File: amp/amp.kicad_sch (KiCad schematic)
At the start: 40 parts, among them J1 Input, J2 Speaker 8Ω, J3 Headphones, J6 FX Send, J7 FX Return, SW1 FX Enable/Bypass, U1 NE5532, U3 LM386

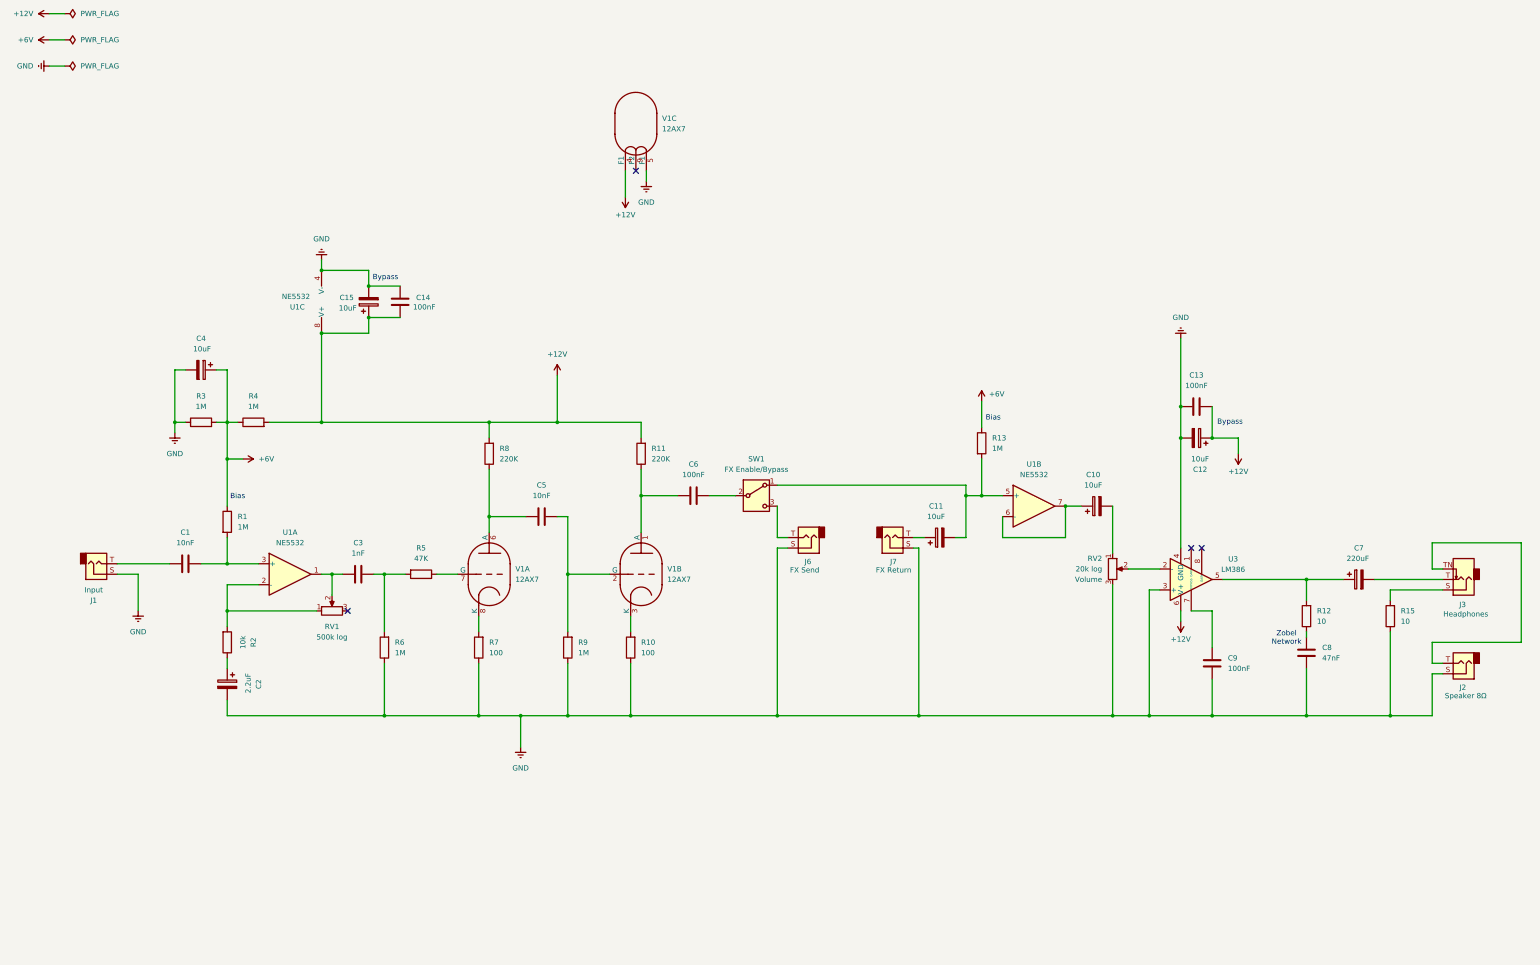
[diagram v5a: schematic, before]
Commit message: Add power control and led indicators
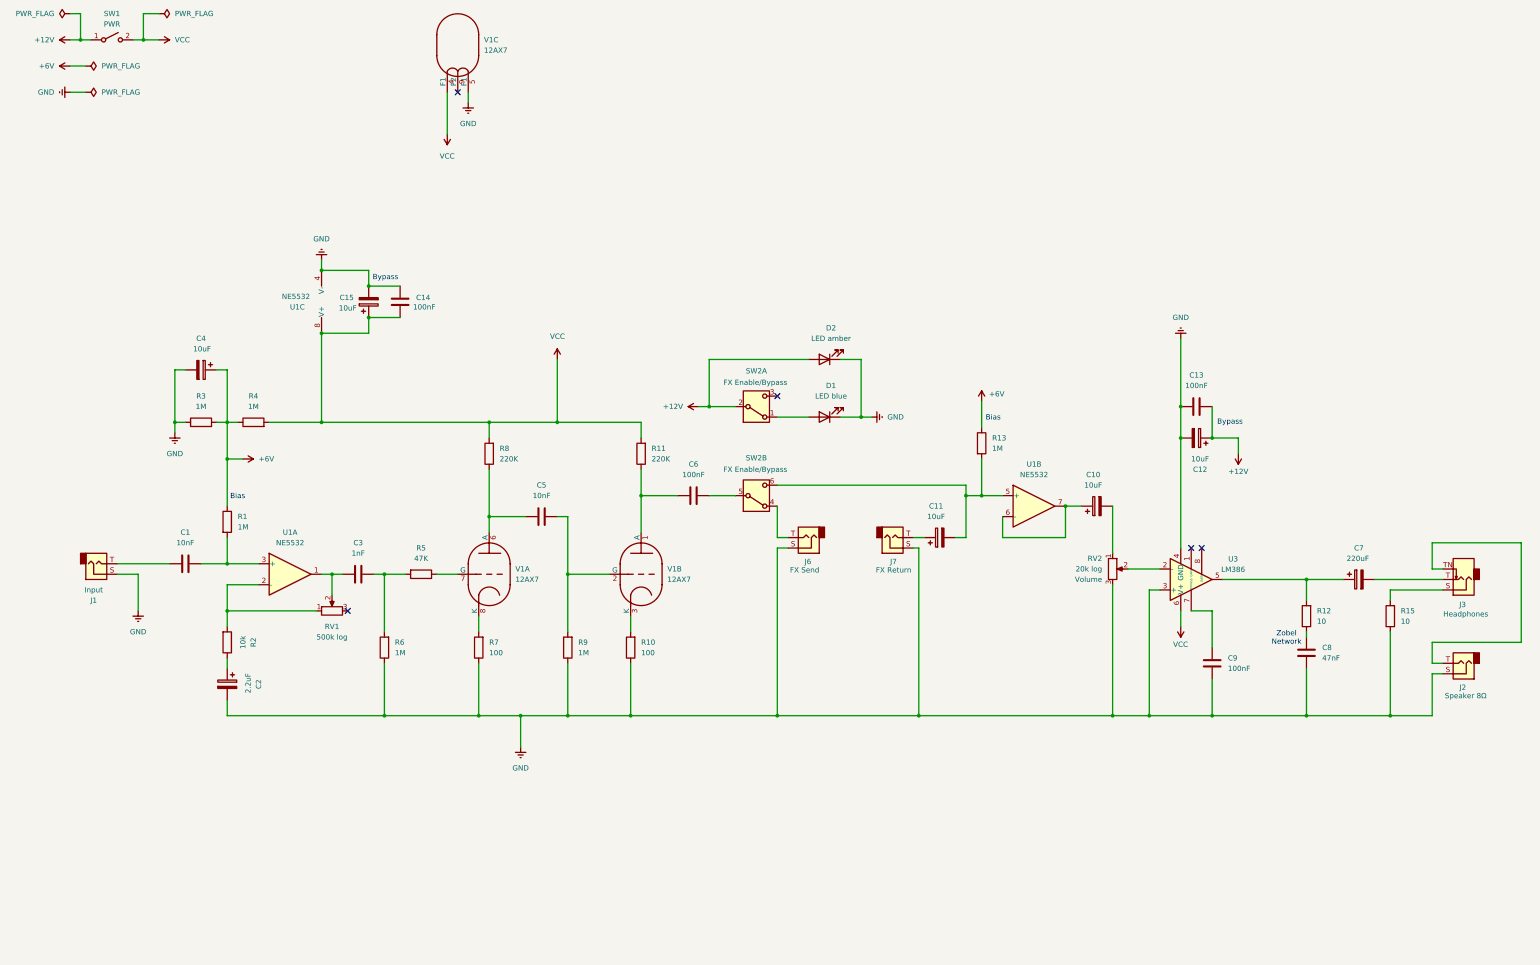
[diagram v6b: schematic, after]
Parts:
- removed SW1: FX Enable/Bypass, symbol Switch:SW_SPDT
- added D1: LED blue, symbol Device:LED
- added D2: LED amber, symbol Device:LED
- added SW1: PWR, symbol Switch:SW_SPST
- added SW2: FX Enable/Bypass, symbol Switch:SW_DPDT_x2
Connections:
- net +12V: now also D2.2 (A), SW1.1 (A), SW2.2 (B); no longer C14.2, C15.1, R11.2, R4.2, R8.2, U1.8 (V+), U3.6 (V+), V1.4 (F1)
- net GND: now also D1.1 (K), D2.1 (K)
- net at J6.T: now also SW2.4 (A)
- net at C6.2: now also SW2.5 (B)
- net at C11.2, R13.2, U1.5 (+): now also SW2.6 (C)
- new net: D1.2 (A), SW2.1 (A)
- new net VCC: C14.2, C15.1, R11.2, R4.2, R8.2, SW1.2 (B), U1.8 (V+), U3.6 (V+), V1.4 (F1)
- no-connect marks 4 -> 5
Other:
- moved on the sheet: V1C

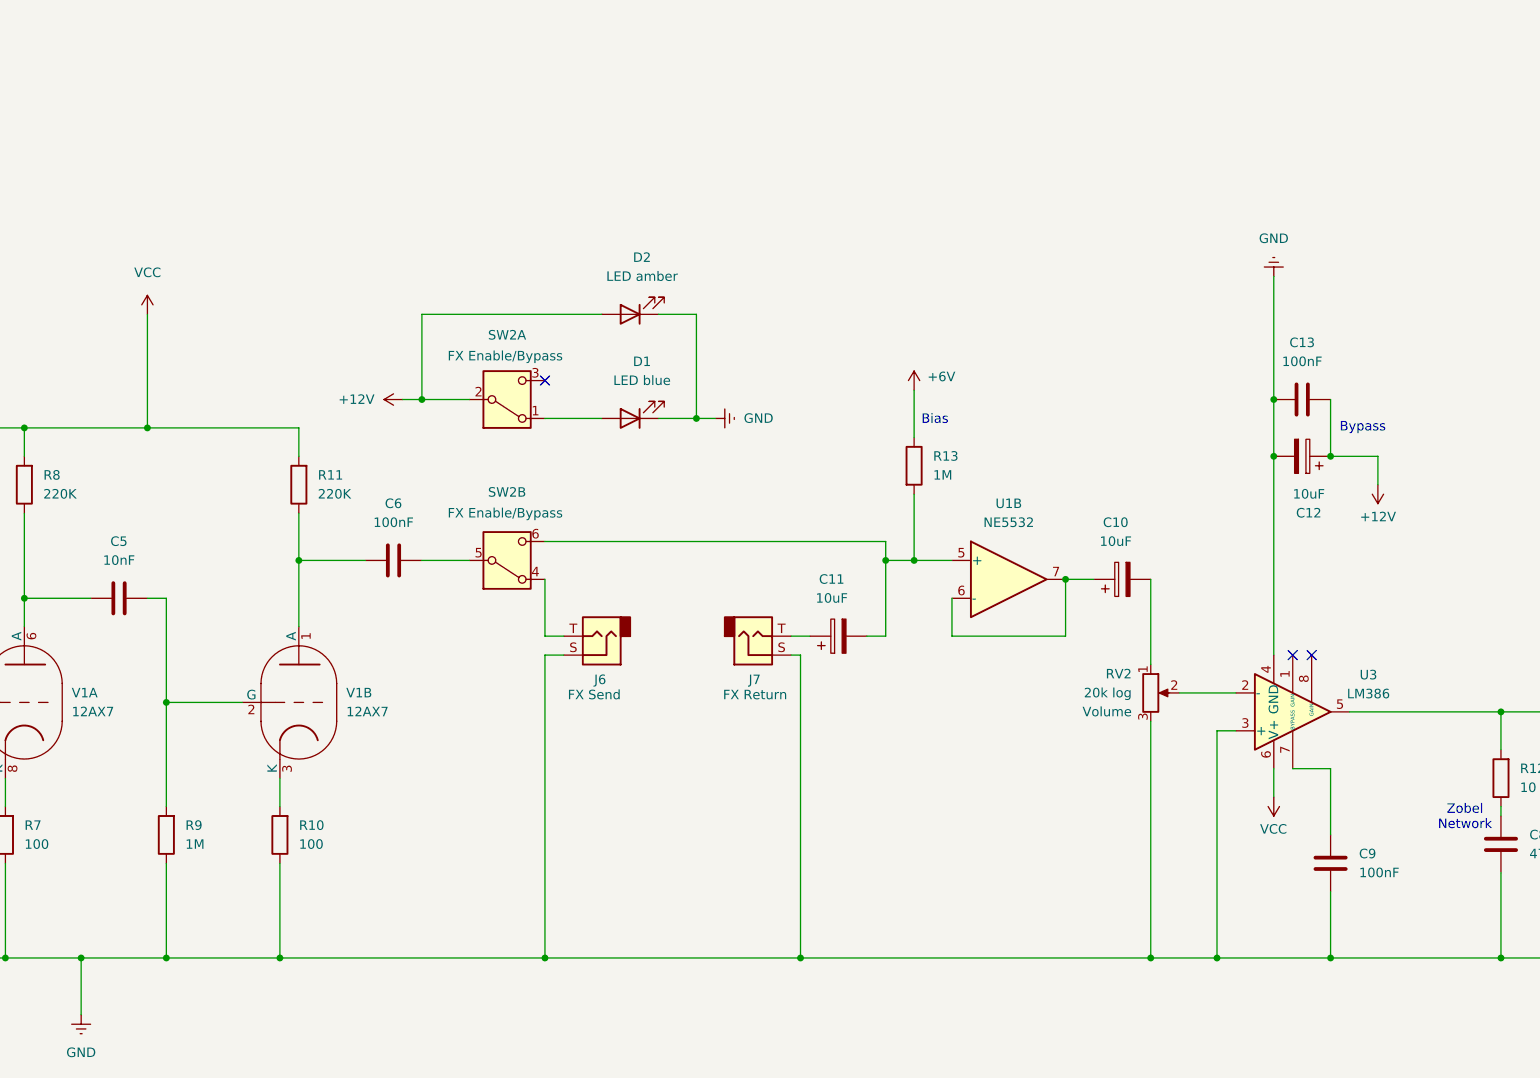
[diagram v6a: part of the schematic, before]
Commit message: Schematic improvements (#14)
- Replace remaining 12V with VCC
- Schematic placement
- TODO updates
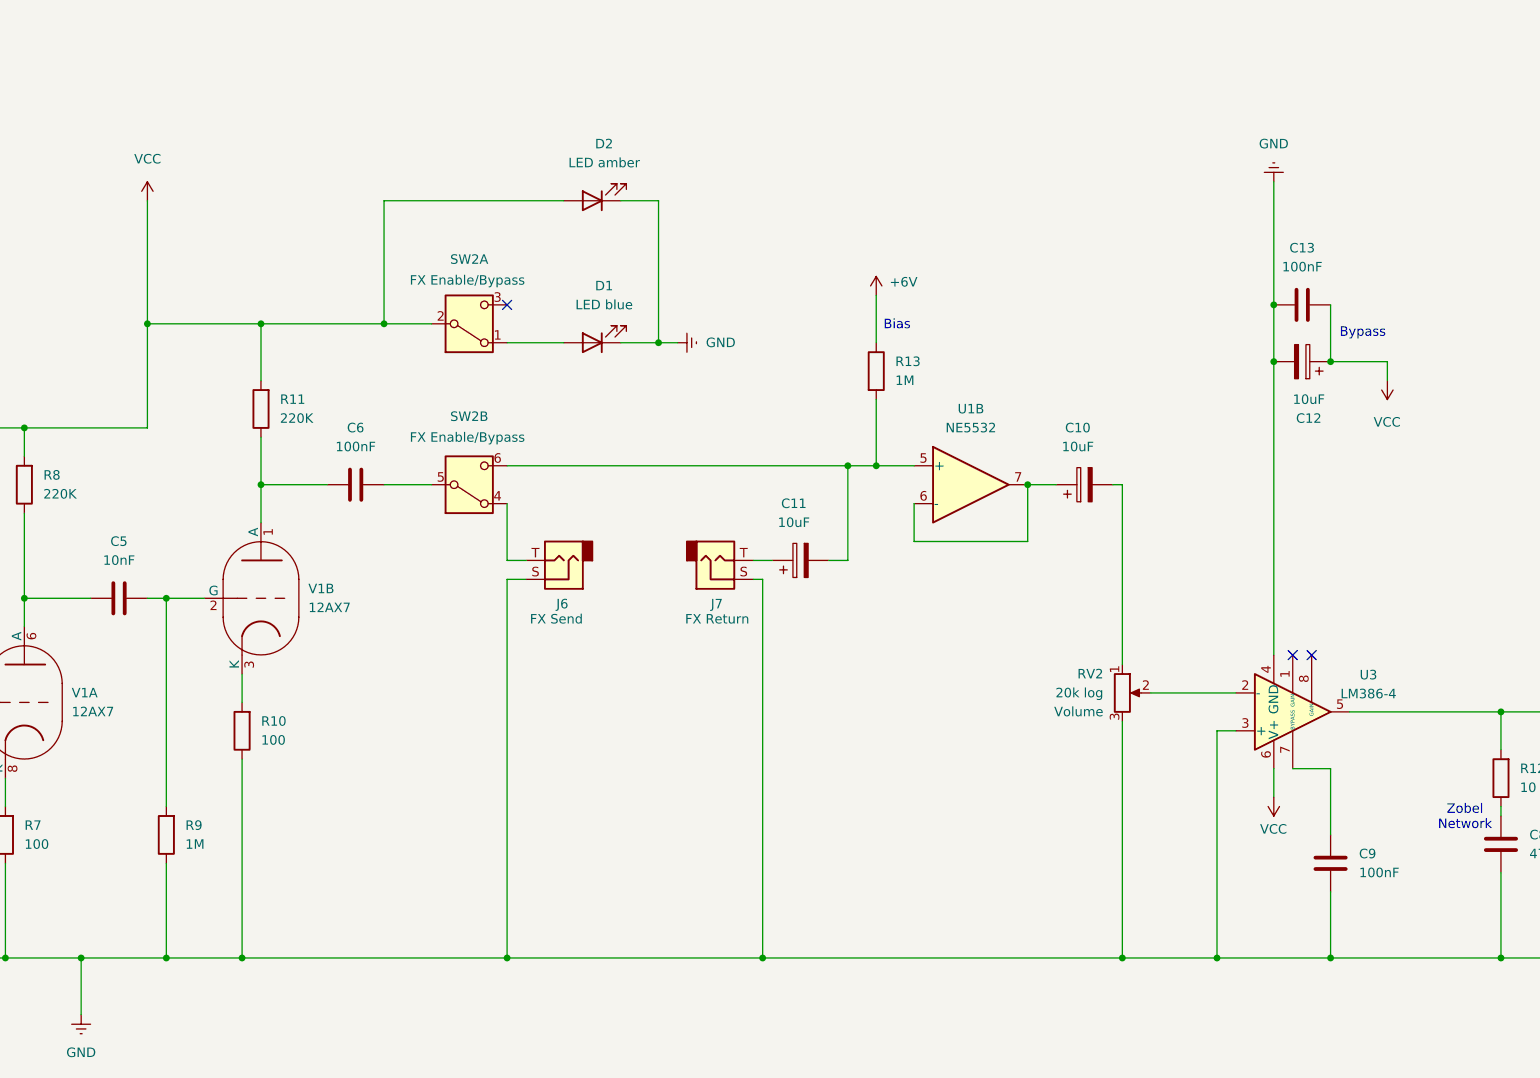
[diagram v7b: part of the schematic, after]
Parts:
- U3: value LM386 -> LM386-4
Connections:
- net +12V: no longer C12.1, C13.2, D2.2 (A), SW2.2 (B)
- net VCC: now also C12.1, C13.2, D2.2 (A), SW2.2 (B)
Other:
- moved on the sheet: C10, C11, C12, C13, C6, D1, D2, J6, J7, R10, R11, R13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

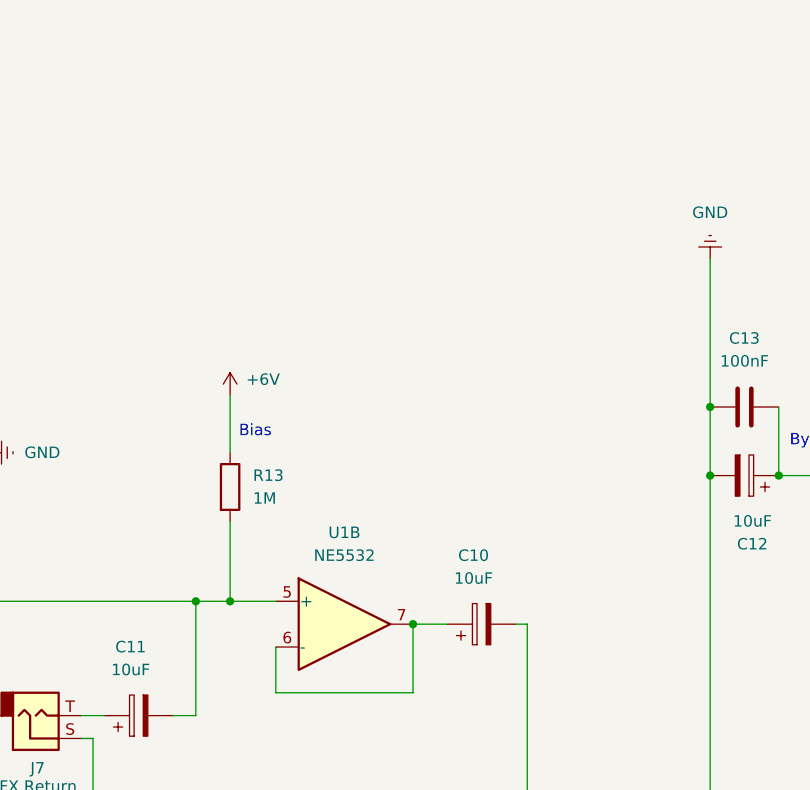
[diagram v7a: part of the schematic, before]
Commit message: Add missing bias after fx loop ret opamp
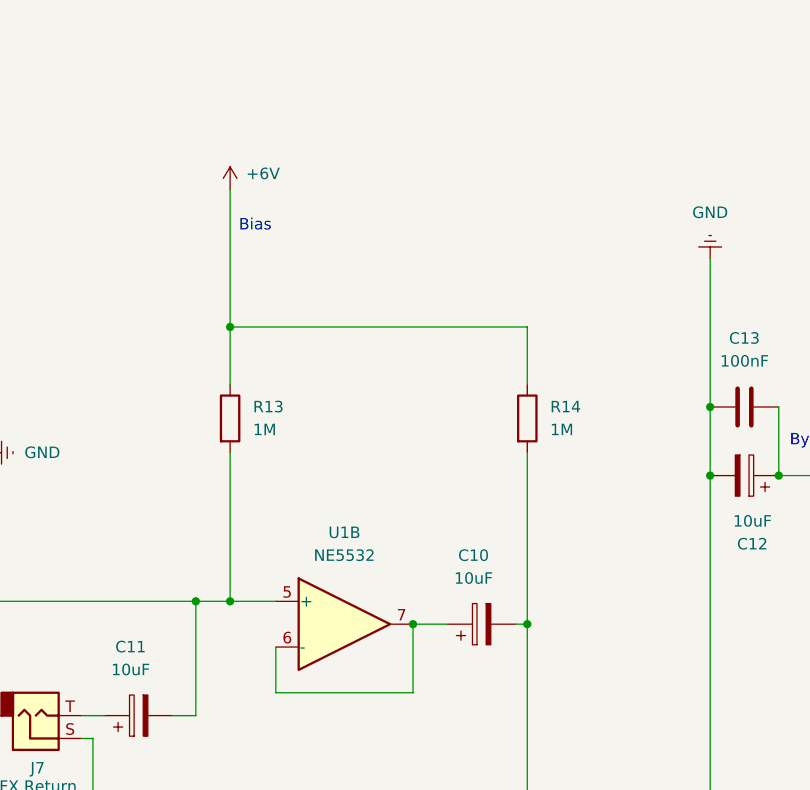
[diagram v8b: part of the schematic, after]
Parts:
- added R14: 1M, symbol Device:R
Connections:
- net +6V: now also R14.1
- net at C10.2, RV2.1: now also R14.2
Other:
- moved on the sheet: R13
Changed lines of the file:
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@@
 	(text "Bias\n"
 		(exclude_from_sim no)
-		(at 249.174 103.124 0)
+		(at 249.174 80.264 0)
 		(effects
 			(font
@@
 	)
 	(junction
+		(at 246.38 91.44)
+		(diameter 0)
+		(color 0 0 0 0)
+	)
+	(junction
 		(at 266.7 124.46)
 		(diameter 0)
@@
 	)
 	(junction
+		(at 279.4 124.46)
+		(diameter 0)
+		(color 0 0 0 0)
+	)
+	(junction
 		(at 129.54 187.96)
 		(diameter 0)
@@
 	(wire
 		(pts
-			(xy 246.38 99.06) (xy 246.38 105.41)
+			(xy 246.38 76.2) (xy 246.38 91.44)
 		)
 		(stroke
@@
 	(wire
 		(pts
+			(xy 246.38 91.44) (xy 279.4 91.44)
+		)
+		(stroke
+			(width 0)
+			(type default)
+		)
+	)
+	(wire
+		(pts
 			(xy 242.57 121.92) (xy 242.57 134.62)
 		)
@@
 	(wire
 		(pts
+			(xy 279.4 105.41) (xy 279.4 124.46)
+		)
+		(stroke
+			(width 0)
+			(type default)
+		)
+	)
+	(wire
+		(pts
 			(xy 246.38 121.92) (xy 251.46 121.92)
 		)
@@
 	(wire
 		(pts
-			(xy 246.38 113.03) (xy 246.38 121.92)
+			(xy 246.38 105.41) (xy 246.38 121.92)
 		)
 		(stroke
@@
 	(wire
 		(pts
+			(xy 246.38 91.44) (xy 246.38 97.79)
+		)
+		(stroke
+			(width 0)
+			(type default)
+		)
+	)
+	(wire
+		(pts
 			(xy 68.58 116.84) (xy 68.58 125.73)
 		)
@@
 	(wire
 		(pts
+			(xy 279.4 97.79) (xy 279.4 91.44)
+		)
+		(stroke
+			(width 0)
+			(type default)
+		)
+	)
+	(wire
+		(pts
 			(xy 330.2 176.53) (xy 330.2 187.96)
 		)
@@
 	(symbol
 		(lib_id "Device:R")
+		(at 279.4 101.6 0)
+		(unit 1)
+		(exclude_from_sim no)
+		(in_bom yes)
+		(on_board yes)
+		(dnp no)
+		(fields_autoplaced yes)
+		(property "Reference" "R14"
+			(at 281.94 100.3299 0)
+			(effects
+				(font
+					(size 1.27 1.27)
+				)
+				(justify left)
+			)
+		)
+		(property "Value" "1M"
+			(at 281.94 102.8699 0)
+			(effects
+				(font
+					(size 1.27 1.27)
+				)
+				(justify left)
+			)
+		)
+		(property "Footprint" ""
+			(at 277.622 101.6 90)
+			(effects
+				(font
+					(size 1.27 1.27)
+				)
+				(hide yes)
+			)
+		)
+		(property "Datasheet" "~"
+			(at 279.4 101.6 0)
+			(effects
+				(font
+					(size 1.27 1.27)
+				)
+				(hide yes)
+			)
+		)
+		(property "Description" "Resistor"
+			(at 279.4 101.6 0)
+			(effects
+				(font
+					(size 1.27 1.27)
+				)
+				(hide yes)
+			)
+		)
+		(pin "2"
+		)
+		(pin "1"
+		)
+		(instances
+			(project "amp"
+				(path "/512e3d9b-1648-4f09-9748-8ed1e9d71853"
+					(reference "R14")
+					(unit 1)
+				)
+			)
+		)
+	)
+	(symbol
+		(lib_id "Device:R")
 		(at 68.58 140.97 0)
 		(unit 1)
@@
 	(symbol
 		(lib_id "power:+6V")
-		(at 246.38 99.06 0)
+		(at 246.38 76.2 0)
 		(unit 1)
 		(exclude_from_sim no)
@@
 		(dnp no)
 		(property "Reference" "#PWR013"
-			(at 246.38 102.87 0)
+			(at 246.38 80.01 0)
 			(effects
 				(font
@@
 		)
 		(property "Value" "+6V"
-			(at 248.158 97.282 0)
+			(at 248.158 74.422 0)
 			(effects
 				(font
@@
 		)
 		(property "Footprint" ""
-			(at 246.38 99.06 0)
+			(at 246.38 76.2 0)
 			(effects
 				(font
@@
 		)
 		(property "Datasheet" ""
-			(at 246.38 99.06 0)
+			(at 246.38 76.2 0)
 			(effects
 				(font
@@
 		)
 		(property "Description" "Power symbol creates a global label with name \"+6V\""
-			(at 246.38 99.06 0)
+			(at 246.38 76.2 0)
 			(effects
 				(font
@@
 	(symbol
 		(lib_id "Device:R")
-		(at 246.38 109.22 0)
+		(at 246.38 101.6 0)
 		(unit 1)
 		(exclude_from_sim no)
@@
 		(fields_autoplaced yes)
 		(property "Reference" "R13"
-			(at 248.92 107.9499 0)
+			(at 248.92 100.3299 0)
 			(effects
 				(font
@@
 		)
 		(property "Value" "1M"
-			(at 248.92 110.4899 0)
+			(at 248.92 102.8699 0)
 			(effects
 				(font
@@
 		)
 		(property "Footprint" ""
-			(at 244.602 109.22 90)
+			(at 244.602 101.6 90)
 			(effects
 				(font
@@
 		)
 		(property "Datasheet" "~"
-			(at 246.38 109.22 0)
+			(at 246.38 101.6 0)
 			(effects
 				(font
@@
 		)
 		(property "Description" "Resistor"
-			(at 246.38 109.22 0)
+			(at 246.38 101.6 0)
 			(effects
 				(font
